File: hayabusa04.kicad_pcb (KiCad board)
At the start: 2 copper layers, 84.1 x 38.1 mm, 24 parts, among them SW1 SW_Push, U1 ATmega32U4-AU, Y1 16MHz

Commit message: routed pcb
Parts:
- moved C7 6.88 mm to (132.0, 81.5), turned to 270 degrees
- moved C4 4.32 mm to (133.2, 67.1)
- moved R3 4.13 mm to (129.2, 67.1), turned to 270 degrees
- moved R2 3.68 mm to (121.0, 67.6)
- moved USB1 3.68 mm to (119.9, 57.3)
- moved F1 3.68 mm to (114.3, 74.9), turned to 90 degrees
- moved R1 3.68 mm to (118.1, 67.6)
- moved SW1 3.68 mm to (120.5, 88.5)
- moved C6 3.60 mm to (132.0, 75.6), turned to 180 degrees
- moved C5 0.83 mm to (146.4, 86.1)
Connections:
- U1 pad 27: Net-(U1-Pad27) -> ROW0
- U1 pad 28: Net-(U1-Pad28) -> COL1
- U1 pad 29: Net-(U1-Pad29) -> COL0
- U1 pad 30: Net-(U1-Pad30) -> ROW1
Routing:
- net GND: track 0.00 -> 155.7 mm
- net +5V: track 0.00 -> 112.1 mm, vias 0 -> 5
- net ROW0: track 0.00 -> 52.3 mm
- net COL1: track 0.00 -> 52.0 mm
- net ROW1: track 0.00 -> 50.9 mm
- net Net-(R3-Pad2): track 0.00 -> 35.6 mm, vias 0 -> 2
- net COL0: track 0.00 -> 32.7 mm
- net Net-(R1-Pad1): track 0.00 -> 25.3 mm
- net Net-(R2-Pad2): track 0.00 -> 24.1 mm
- net VCC: track 0.00 -> 13.4 mm
- net Net-(C3-Pad1): track 0.00 -> 13.3 mm
- net Net-(C2-Pad1): track 0.00 -> 10.9 mm
- net Net-(D3-Pad2): track 0.00 -> 6.62 mm
- net Net-(D1-Pad2): track 0.00 -> 6.62 mm
- net Net-(D4-Pad2): track 0.00 -> 6.62 mm
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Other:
- board size 84.1 x 38.1 mm -> 81.8 x 38.1 mm

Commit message: updated pcb
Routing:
- added copper zone on B.Cu, net GND
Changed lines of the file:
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@@
   (segment (start 152.136 80.67) (end 152.2095 80.5965) (width 0.254) (layer B.Cu) (net 20))
   (segment (start 147.8915 80.67) (end 152.136 80.67) (width 0.254) (layer B.Cu) (net 20))
+  (zone (net 1) (net_name GND) (layer B.Cu) (hatch edge 0.508)
+    (connect_pads (clearance 0.508))
+    (min_thickness 0.254)
+    (fill yes (arc_segments 32) (thermal_gap 0.508) (thermal_bridge_width 0.508))
+    (polygon
+      (pts
+        (xy 110.33125 55.5625) (xy 153.9875 55.5625) (xy 153.9875 93.6625) (xy 110.33125 93.6625)
+      )
+    )
+  )
 )

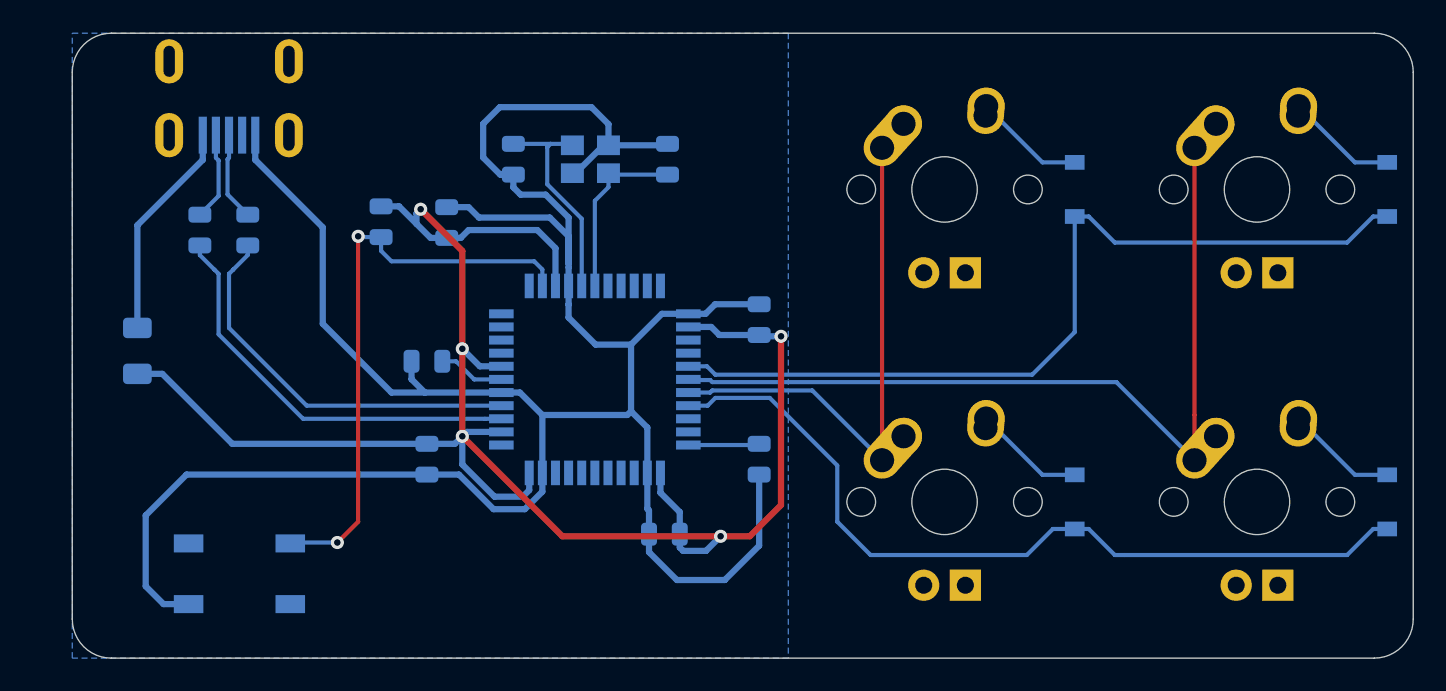
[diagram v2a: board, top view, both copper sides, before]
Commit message: hotswap compatible
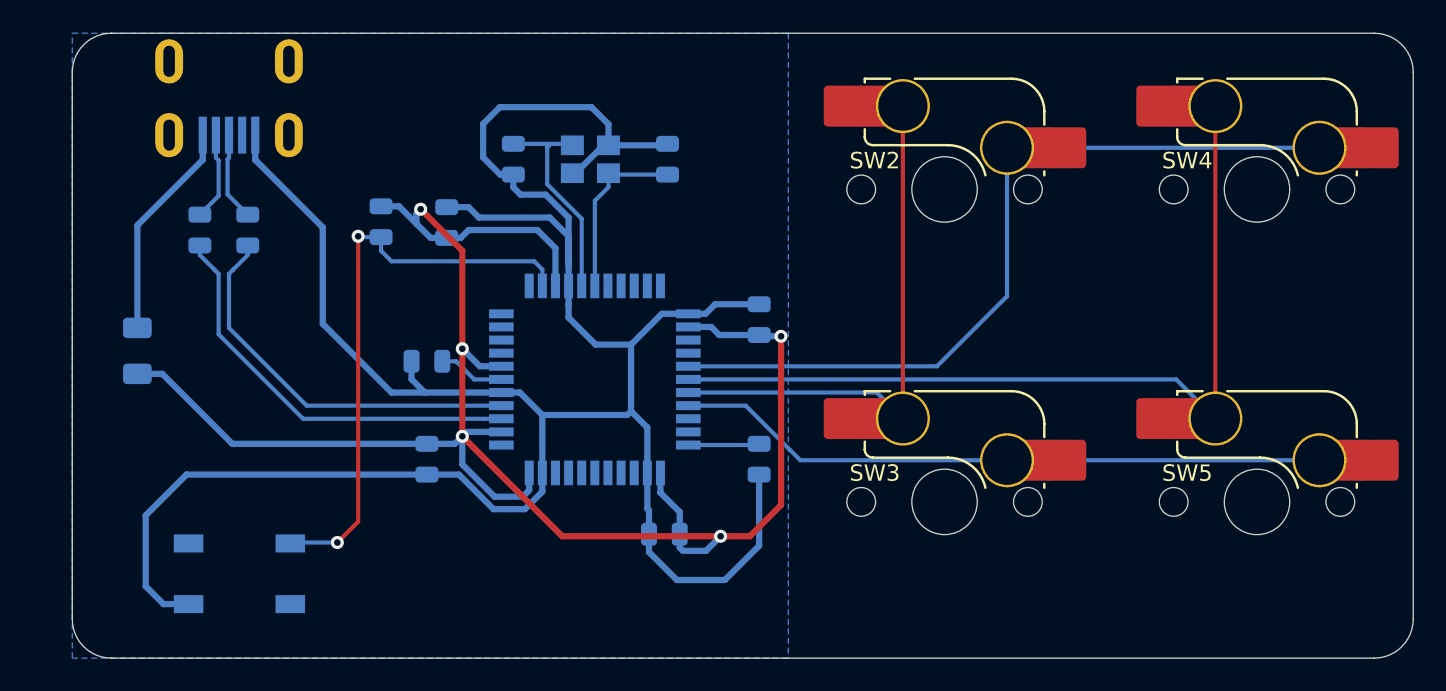
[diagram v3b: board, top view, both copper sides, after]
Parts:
- removed D1, D2, D3, D4: D_Small, Diode_SMD:D_SOD-123
- removed MX1, MX2, MX3, MX4: MX-NoLED, MX_Alps_Hybrid:MX-1U
- added SW2: MX_SW_HS, marbastlib-mx:SW_MX_HS_1u, F.Cu at (163.5, 65.1)
- added SW3: MX_SW_HS, marbastlib-mx:SW_MX_HS_1u, F.Cu at (163.5, 84.1)
- added SW4: MX_SW_HS, marbastlib-mx:SW_MX_HS_1u, F.Cu at (182.6, 65.1)
- added SW5: MX_SW_HS, marbastlib-mx:SW_MX_HS_1u, F.Cu at (182.6, 84.1)
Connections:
- U1 pad 1: Net-(U1-Pad1) -> unconnected-(U1-Pad1)
- U1 pad 10: Net-(U1-Pad10) -> unconnected-(U1-Pad10)
- U1 pad 11: Net-(U1-Pad11) -> unconnected-(U1-Pad11)
- U1 pad 12: Net-(U1-Pad12) -> unconnected-(U1-Pad12)
- U1 pad 18: Net-(U1-Pad18) -> unconnected-(U1-Pad18)
- U1 pad 19: Net-(U1-Pad19) -> unconnected-(U1-Pad19)
- U1 pad 20: Net-(U1-Pad20) -> unconnected-(U1-Pad20)
- U1 pad 21: Net-(U1-Pad21) -> unconnected-(U1-Pad21)
- U1 pad 22: Net-(U1-Pad22) -> unconnected-(U1-Pad22)
- U1 pad 25: Net-(U1-Pad25) -> unconnected-(U1-Pad25)
- U1 pad 26: Net-(U1-Pad26) -> unconnected-(U1-Pad26)
- U1 pad 31: Net-(U1-Pad31) -> unconnected-(U1-Pad31)
- U1 pad 32: Net-(U1-Pad32) -> unconnected-(U1-Pad32)
- U1 pad 36: Net-(U1-Pad36) -> unconnected-(U1-Pad36)
- U1 pad 37: Net-(U1-Pad37) -> unconnected-(U1-Pad37)
- U1 pad 38: Net-(U1-Pad38) -> unconnected-(U1-Pad38)
- U1 pad 39: Net-(U1-Pad39) -> unconnected-(U1-Pad39)
- U1 pad 40: Net-(U1-Pad40) -> unconnected-(U1-Pad40)
- U1 pad 41: Net-(U1-Pad41) -> unconnected-(U1-Pad41)
- U1 pad 42: Net-(U1-Pad42) -> unconnected-(U1-Pad42)
- U1 pad 8: Net-(U1-Pad8) -> unconnected-(U1-Pad8)
- U1 pad 9: Net-(U1-Pad9) -> unconnected-(U1-Pad9)
- USB1 pad 2: Net-(USB1-Pad2) -> unconnected-(USB1-Pad2)
- USB1 pad 6: Net-(USB1-Pad6) -> unconnected-(USB1-Pad6)
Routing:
- net ROW1: track 50.9 -> 39.9 mm
- net Net-(D3-Pad2): track 6.62 -> 0.00 mm
- net Net-(D1-Pad2): track 6.62 -> 0.00 mm
- net Net-(D4-Pad2): track 6.62 -> 0.00 mm
- net Net-(D2-Pad2): track 6.62 -> 0.00 mm
- net COL1: track 52.0 -> 52.9 mm
- net ROW0: track 52.3 -> 52.8 mm
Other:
- net class Default removed
- net class Power removed
